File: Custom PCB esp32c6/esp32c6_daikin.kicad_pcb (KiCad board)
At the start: 2 copper layers, 40 x 25 mm, 26 parts, among them J2 Conn_01x05, Q1 BSS138PS, U1 TPS562246, U2 XIAO-ESP32-C6

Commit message: fix(xiao-pcb): move center-gap passives out of antenna keep-out
Re-review flagged R1, R2, C16 as a Task 7 placement defect, not a Task 8
routing note: parts sitting under the antenna region is poor RF practice
independent of the keepout's tracks/copperpour ban. Verified by geometry
(pad + courtyard bboxes vs the keepout polygon, both rule-area rects) that
these three were the complete offender set beyond U2 itself.

Relocated, preserving layer/orientation:
- R1 (5V_BUCK/HV1, shifter HV-side pull-up) to (177.147,106.118), next to
  the Q1/R10/R11 shifter cluster it belongs to.
- R2 (3V3/TX1 pull-up) to (152.089,108.891), just off U2's bottom edge,
  ~2.4mm from the TX1 pad it serves, clear of the keepout and of U2's own
  pad copper.
- C16 (V_in/GND) to (182.279,89.243), immediately adjacent to U1 (buck
  regulator) pad 1 (V_in) -- it decouples U1, so it now sits at the IC
  it serves rather than orphaned in the antenna region.

All three positions found by scanning real pad-copper extents (not
silkscreen-inflated bounding boxes) for gaps clear of every other
footprint's copper and of both keepout rule-area rectangles with margin.
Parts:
- moved C16 29.8 mm to (182.3, 89.2)
- moved R1 23.6 mm to (177.1, 106.1)
- moved R2 15.9 mm to (152.1, 108.9)
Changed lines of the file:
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@@
 	(footprint "easyeda2kicad:R0402"
 		(layer "F.Cu")
-		(at 153.7 103.480384 90)
+		(at 177.147 106.118 90)
 		(property "Reference" "R1"
 			(at 0 -4 90)
@@
 	(footprint "easyeda2kicad:R0402"
 		(layer "F.Cu")
-		(at 154.259807 93.15)
+		(at 152.089 108.891)
 		(property "Reference" "R2"
 			(at 0 -4 0)
@@
 	(footprint "easyeda2kicad:C0402"
 		(layer "F.Cu")
-		(at 154 98.5 90)
+		(at 182.279 89.243 90)
 		(property "Reference" "C16"
 			(at 0 -4 90)
@@
 		(polygon
 			(pts
-				(xy 146 90) (xy 150.3 90) (xy 150.3 92.2) (xy 155.5 92.2) (xy 155.5 104.8) (xy 150.3 104.8) (xy 150.3 107) (xy 146 107)
+				(xy 146 90) (xy 150.3 90) (xy 150.3 92.2) (xy 155.5 92.2) (xy 155.5 104.8) (xy 150.3 104.8) (xy 150.3 107)
+				(xy 146 107)
 			)
 		)

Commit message: fix(xiao-pcb): re-place buck support passives per datasheet layout
Move C3/C17 input caps, C18 bootstrap, R6/R8/C19 feedback divider,
C15 output cap tight to U1/L1 in the top-right buck cluster; C20 VBUS
cap to the XIAO VBUS pin; R12 pull-up to the HV2 node at Q1/R11.
Clears the XIAO center-gap of buck nets (root cause of the prior
2-net routing block) and shortens SW/bootstrap/feedback loops per the
TPS562246 layout guidance. Placement DRC (courtyard/short) clean.
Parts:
- moved C15 25.2 mm to (184.5, 93.0), turned to 0 degrees
- moved C18 23.9 mm to (180.7, 91.0), turned to 0 degrees
- moved C3 22.1 mm to (180.9, 87.0), turned to 180 degrees
- moved R5 19.1 mm to (177.5, 92.5), turned to 0 degrees
- moved R8 18.4 mm to (180.7, 92.8), turned to 180 degrees
- moved C19 17.0 mm to (180.7, 91.9), turned to 180 degrees
- moved R12 16.9 mm to (174.5, 101.6)
- moved C20 11.7 mm to (170.0, 92.3), turned to 0 degrees
- moved C17 8.33 mm to (174.0, 96.5), turned to 0 degrees
- moved R6 6.08 mm to (180.7, 93.8)

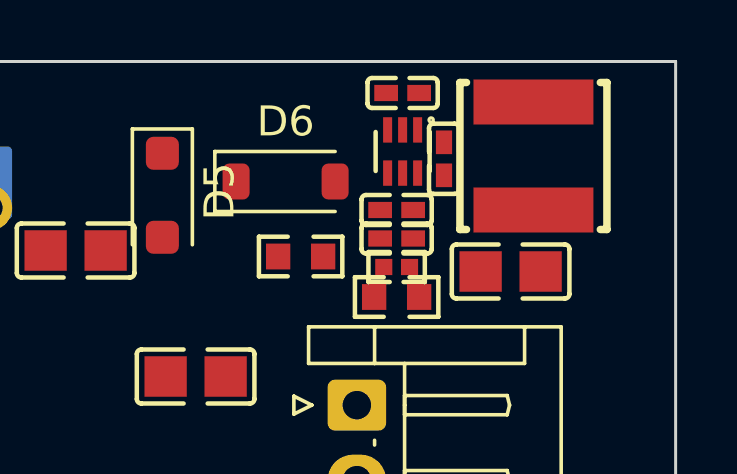
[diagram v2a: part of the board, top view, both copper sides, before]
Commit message: fix(xiao-pcb): unseal U1 VFB pad exit (nudge C16 east 0.4mm)
The VFB sense pin U1-6 was physically sealed at OSH Park 6-mil clearance:
its only lateral exit (rightward) was pinched between the C18-2/SW pad halo
(right edge 181.645, +0.2286 halo = 181.874) and the C16-1/V_in pad halo
(left edge 182.009, -0.2286 halo = 181.780). The two halos overlapped
(181.780 < 181.874), leaving no gap, so no trace or via could leave the pad.
Three independent routers (maze, Freerouting push-shove x10 runs, A* finisher)
plus closed-form geometry all confirmed U1-6 could not be exited.

Fix: move C16 (VIN input decoupler) 0.4mm east, 182.279 -> 182.679 (x only,
y unchanged). This opens a 0.306mm (2x trace-width) descent corridor on the
right of C18-2: window x[181.874, 182.180]. C16 stays the closest VIN
decoupler to U1-1. C18 (bootstrap) is untouched, staying tight to BOOT-SW.
C16 has ~0.7mm pad clearance eastward (L1-2 at y[90.2,91.7] does not y-overlap
C16 at y<90.19), so the move is unconstrained by neighbors.

Placement DRC (courtyard + clearance): 0 violations. Positions only; nothing
in the antenna keep-out. Validated: U1-6 VFB now routes (A* finisher, 5 segs,
0 vias) at 0.1524mm OSH Park clearance where before it reached 0 cells off-pad.
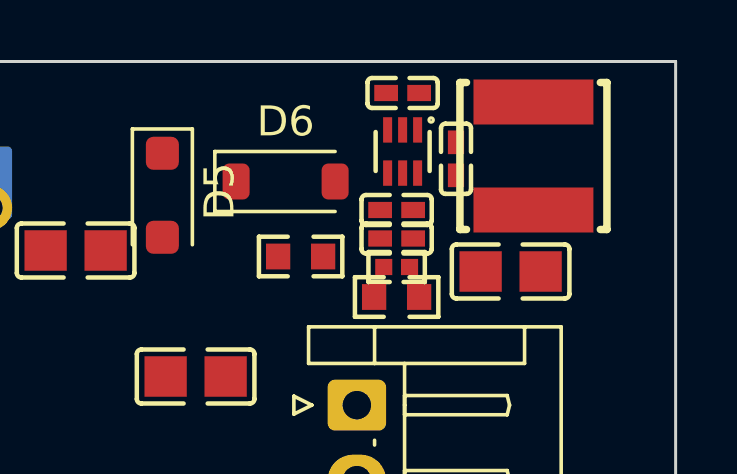
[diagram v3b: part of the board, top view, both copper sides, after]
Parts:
- moved C16 0.40 mm to (182.7, 89.2)
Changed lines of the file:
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@@
 	(footprint "easyeda2kicad:C0402"
 		(layer "F.Cu")
-		(at 182.279 89.243 90)
+		(at 182.679 89.243 90)
 		(property "Reference" "C16"
 			(at 0 -4 90)

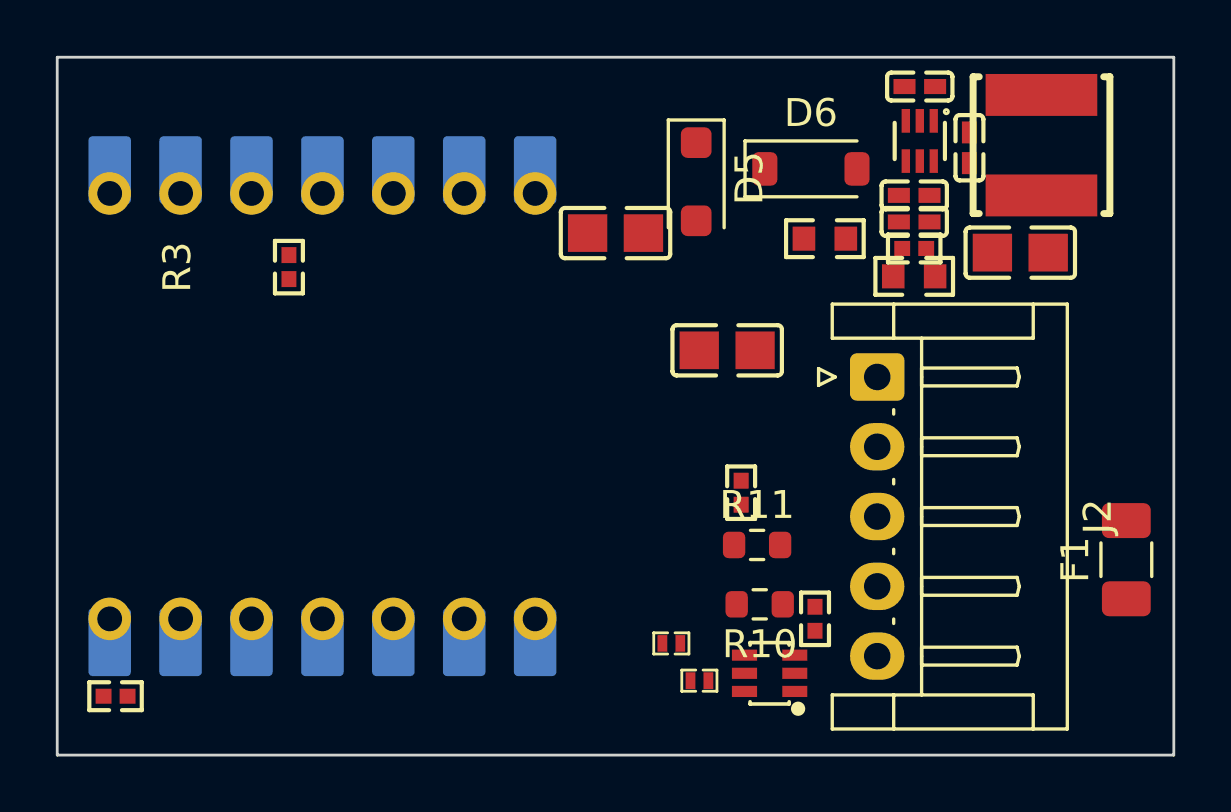
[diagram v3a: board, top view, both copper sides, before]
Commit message: fix(xiao-pcb): re-layout buck cluster with per-net routing corridors
The TPS562246 (U1, SOT-23-6, 0.5mm pitch) buck cluster could not route at
the board's 0.2mm track-to-pad DRU rule: three middle/edge pins (SW, EN, VFB)
over-subscribed a single ~0.3mm corridor. Re-laid out the cluster so each hard
pin gets its own >=0.2mm-clean escape, budgeted geometrically before placing.

U1 kept at 180.9,89.0 rot90; corridors cleared:
- SW (U1-2, top-mid) exits up into a clear strip y[86.5,87.8]  -> C3 moved off
  the SW column: C3 180.9,87.05 -> 181.9,86.9 (VIN cap now above VIN pin U1-1).
- EN (U1-5) / VFB (U1-6) / VBST (U1-4) exit down into a cleared fan-band
  y[90.3,92.3] -> the FB divider + bootstrap moved out of the immediate band:
  C18 (bootstrap) 180.7,90.95 -> 179.0,88.7 (left of U1, tight across BOOT-SW);
  C19 -> 181.3,92.6, R8 -> 181.3,93.8, R6 -> 183.4,93.4 (FB divider below VFB,
  kept away from the SW/L1 switching node per TI layout guidance);
  R5 (EN pull-up) 177.5,92.5 -> 178.3,92.8.
- Input/output spread to clear the fan-bands: C16 -> 183.3,89.5; L1 186.4,89.15;
  C15 -> 186.65,93.3 (also opens a 6-mil pad gap to R6-2); D6 -> 176.1,90.0;
  D5 -> 172.2,90.4; C20 -> 169.8,93.4; C17 -> 173.5,96.0.

TI TPS562246 datasheet layout section (SLVSFH9): keep SW short/wide and route
switching current away from the device; make the FB node small and away from
the SW trace; input caps tight to VIN-GND. This layout follows all three.

U2/J2/Q1-cluster and the antenna keep-out polygon are untouched. Placement DRC
(courtyard + clearance, board's own rules): 0 violations.
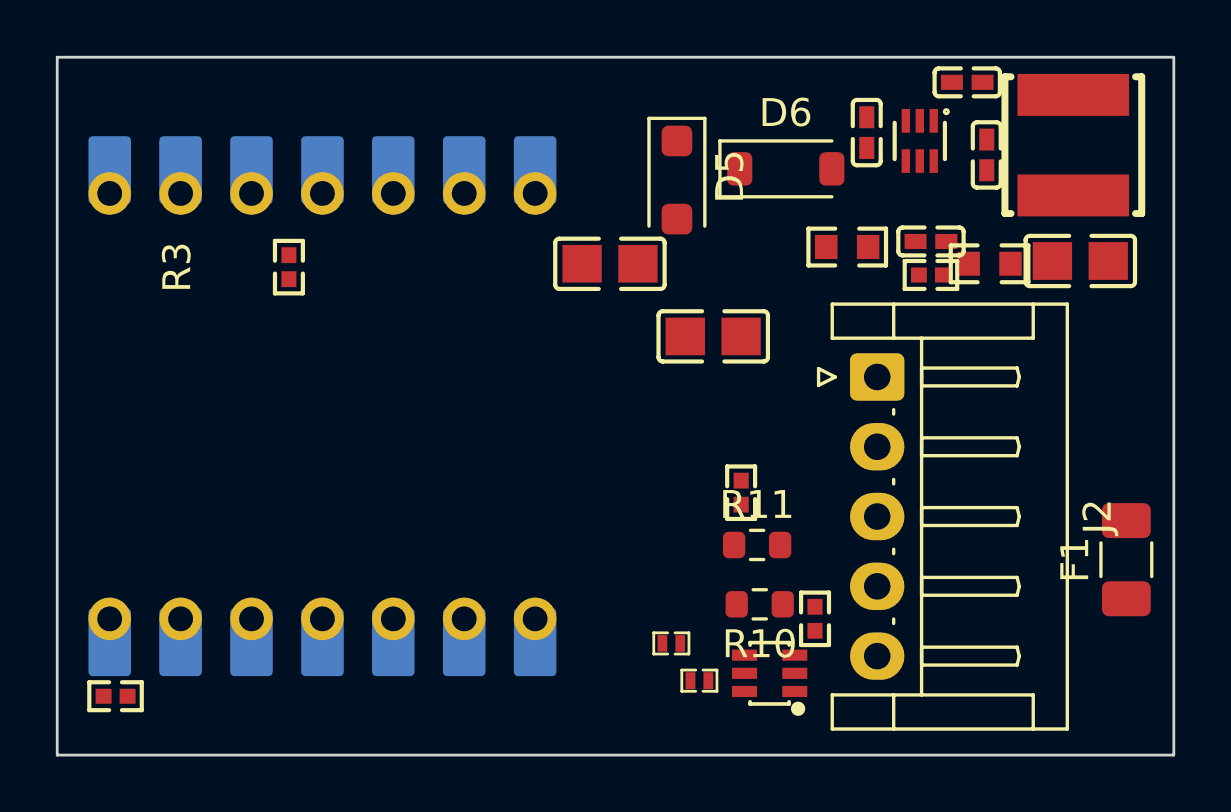
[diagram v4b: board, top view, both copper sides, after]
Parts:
- moved C18 2.82 mm to (179.0, 88.7), turned to 90 degrees
- moved R6 2.74 mm to (183.4, 93.4)
- moved C15 2.17 mm to (186.7, 93.3)
- moved C3 1.71 mm to (182.6, 86.9), turned to 0 degrees
- moved L1 1.14 mm to (186.4, 89.2)
- moved R8 1.12 mm to (181.3, 93.8), turned to 0 degrees
- moved C20 1.12 mm to (169.8, 93.4)
- moved C19 0.92 mm to (181.3, 92.6), turned to 0 degrees
- moved D6 0.90 mm to (176.1, 90.0)
- moved R5 0.85 mm to (178.3, 92.8)
- moved C17 0.71 mm to (173.5, 96.0)
- moved D5 0.69 mm to (172.2, 90.4)
- moved C16 0.67 mm to (183.3, 89.5)

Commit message: feat(xiao-pcb): route, pour, DRC clean, OSH Park 6-mil verified
Full 2-layer routing on the re-laid-out buck cluster. All 15 signal/power nets
route at the board's own DRU rules (0.2mm track-to-pad, 0.127mm track-track,
0.33mm track-to-hole, 0.3mm edge). Power nets (5V_BUCK, VBUS, V_in, 12V_IN)
on a Power netclass at 0.3mm width. Antenna keep-out respected (no tracks in
the polygon); TX1/RX1 escape through the keep-out notch; S21 traces clear of L1.

GND: solid pour both layers, stitched with vias, single connected plane tied to
the star point J2-5; F.Cu island under the buck output tied through a via.

Toolchain (portable, not committed): Freerouting 2.2.4 on Temurin JRE 25.0.3+9,
DSN/SES via pcbnew ExportSpecctraDSN/ImportSpecctraSES; residual pin-escapes and
keep-out-aware reroutes finished with a pcbnew A* pass; ZONE_FILLER.Fill for the
pour (kicad-cli --refill-zones not used).

Gating DRC (board's own rules, --severity-error): 0 violations, 0 unconnected
(verification/xiao-task8-drc.json).
OSH Park 6-mil check (all clearance rules patched to 0.1524mm on a copy):
0 violations, 0 unconnected.
Renders: verification/xiao-task8-front.png, xiao-task8-back.png (gitignored).
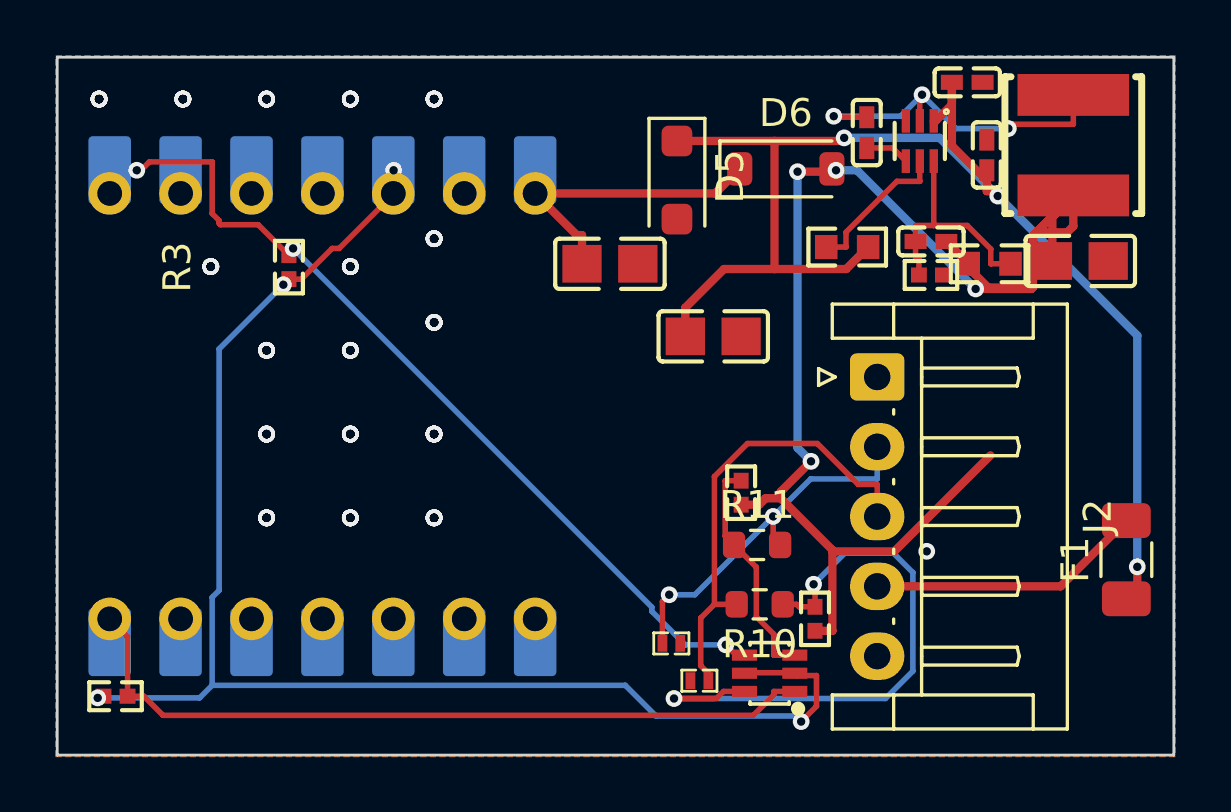
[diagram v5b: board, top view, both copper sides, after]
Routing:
- net /5V_BUCK: track 0.00 -> 56.0 mm, vias 0 -> 4
- net 3V3: track 0.00 -> 52.2 mm, vias 0 -> 4
- net V_in: track 0.00 -> 49.1 mm, vias 0 -> 3
- net RX1: track 0.00 -> 31.6 mm, vias 0 -> 3
- net TX1: track 0.00 -> 28.5 mm
- net /HV1: track 0.00 -> 21.5 mm, vias 0 -> 2
- net /S21_RX_CONN: track 0.00 -> 16.5 mm
- net /S21_TX_CONN: track 0.00 -> 13.3 mm, vias 0 -> 2
- net Net-(U1-SW): track 0.00 -> 12.7 mm, vias 0 -> 3
- net /VBUS: track 0.00 -> 11.9 mm
- net /12V_IN: track 0.00 -> 9.90 mm
- net Net-(U1-VFB): track 0.00 -> 8.45 mm
- net /HV2: track 0.00 -> 8.29 mm
- net Net-(U1-EN): track 0.00 -> 5.36 mm
- net Net-(U1-VBST): track 0.00 -> 1.59 mm
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- added copper zone on B.Cu, net GND
- added copper zone on F.Cu, net GND

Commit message: review(xiao-pcb): delegated DFM review
Apply the two required fixes from the delegated pcb-dfm-reviewer pass
(verification/xiao-pcb-review.md, verdict READY-WITH-FIXES) before
gerber export.

F1: dedupe stacked stitching vias. 17 GND stitch points each carried
6 co-located identical vias (0.3mm drill / 0.6mm pad), 85 redundant
drill hits total. Kept one via per location: 124 -> 39 vias (17 GND
stitch + 22 signal). Eliminates all 199 holes_co_located warnings.

F2: delete dangling stub on /5V_BUCK. Removed the reviewer-identified
4.868mm F.Cu run (183.432,100.262)-(179.989,103.705). Deleting it
exposed a second segment (179.989,103.705)-(177.769,103.705), 2.221mm,
that was only "terminated" by touching the first stub and became newly
dangling once it was gone; removed that too since it is the same
redundant branch (net stays fully connected without either segment,
0 unconnected before and after). Eliminates the 1 track_dangling
warning.

F12 copper-to-edge confirmed 0.5mm (kicad_pro min_copper_edge_clearance),
above the 0.25mm floor, no change needed.

Zones refilled after the edits (pcbnew ZONE_FILLER); GND pour verified
still a single polygon per layer on F.Cu/B.Cu, still tied to J2 pin 5.

Re-verified: gating DRC (severity-error) 0 violations / 0 unconnected
(verification/xiao-task8-drc.json). OSH Park 6-mil DRU+netclass
clearance floor (0.1524mm) re-run per the documented method: 0/0
(verification/xiao-task8-6mil-drc.json). Full-severity warning count
315 -> 115, all remaining categories byte-identical before/after.
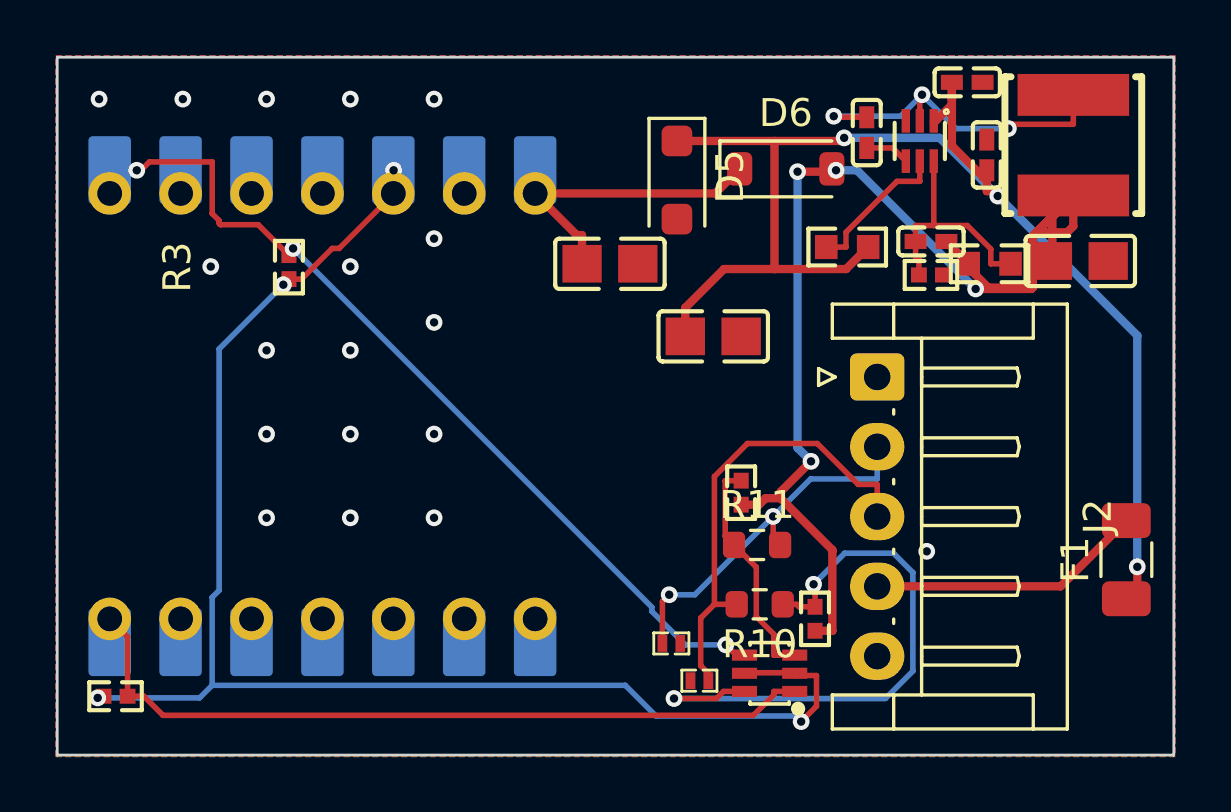
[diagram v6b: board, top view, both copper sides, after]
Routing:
- net /5V_BUCK: track 56.0 -> 48.9 mm
- net GND: vias 103 -> 18
